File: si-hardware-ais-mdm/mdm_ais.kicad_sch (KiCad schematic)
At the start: 11 parts, among them U3 Si4362, Y1 30MHz

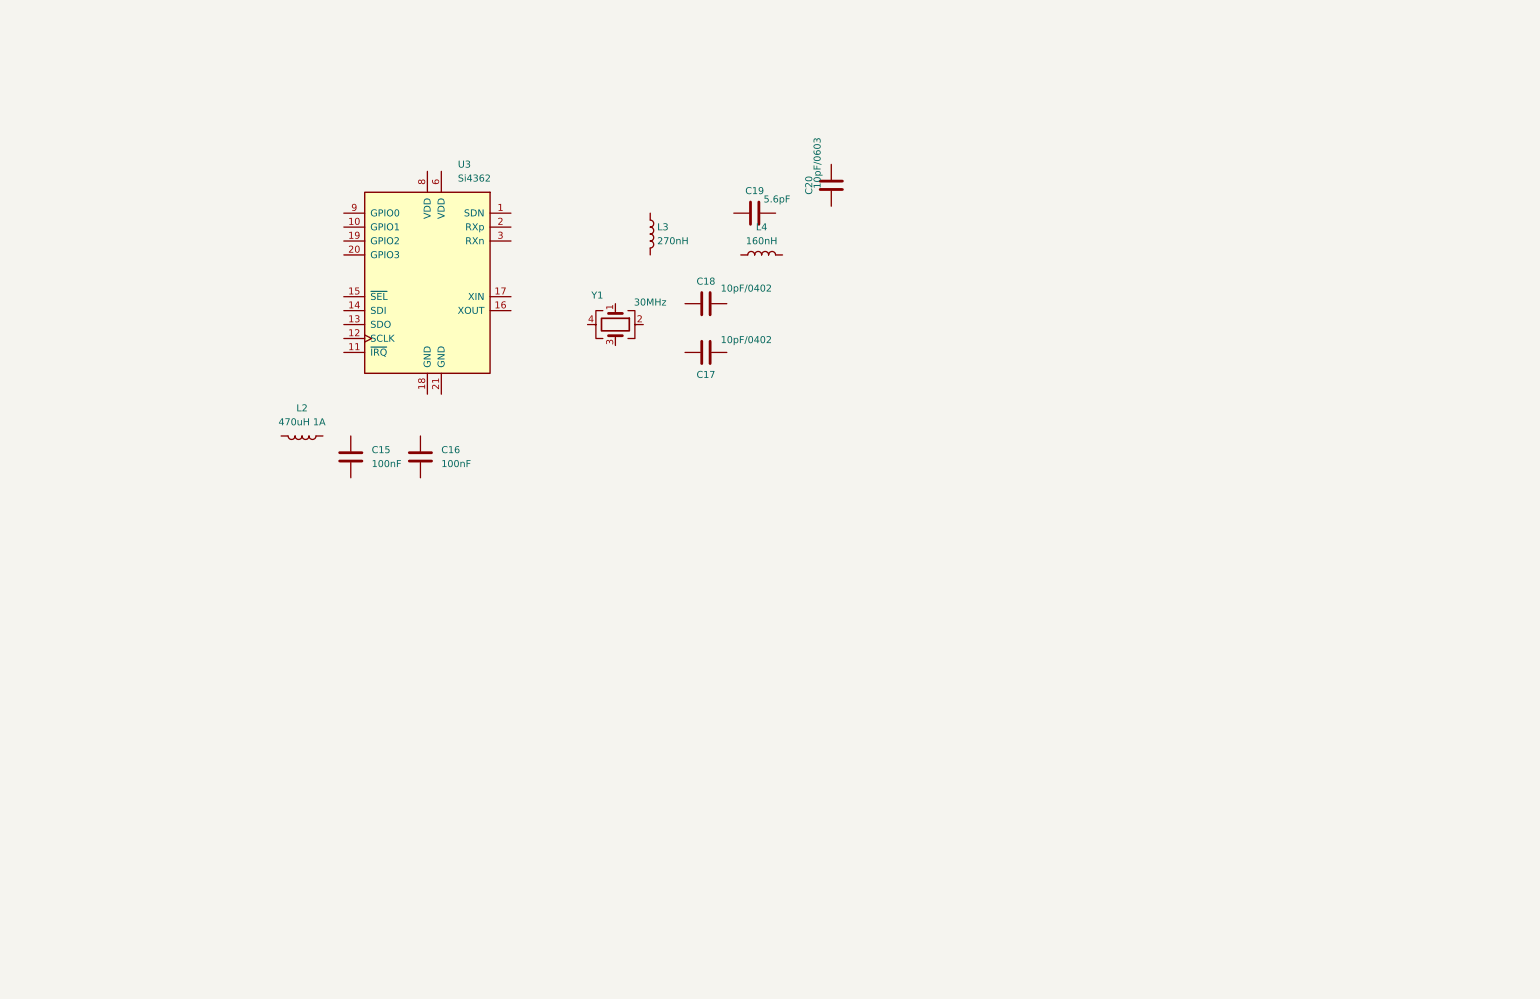
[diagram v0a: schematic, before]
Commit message: added function power input battery chargger mdm_ais
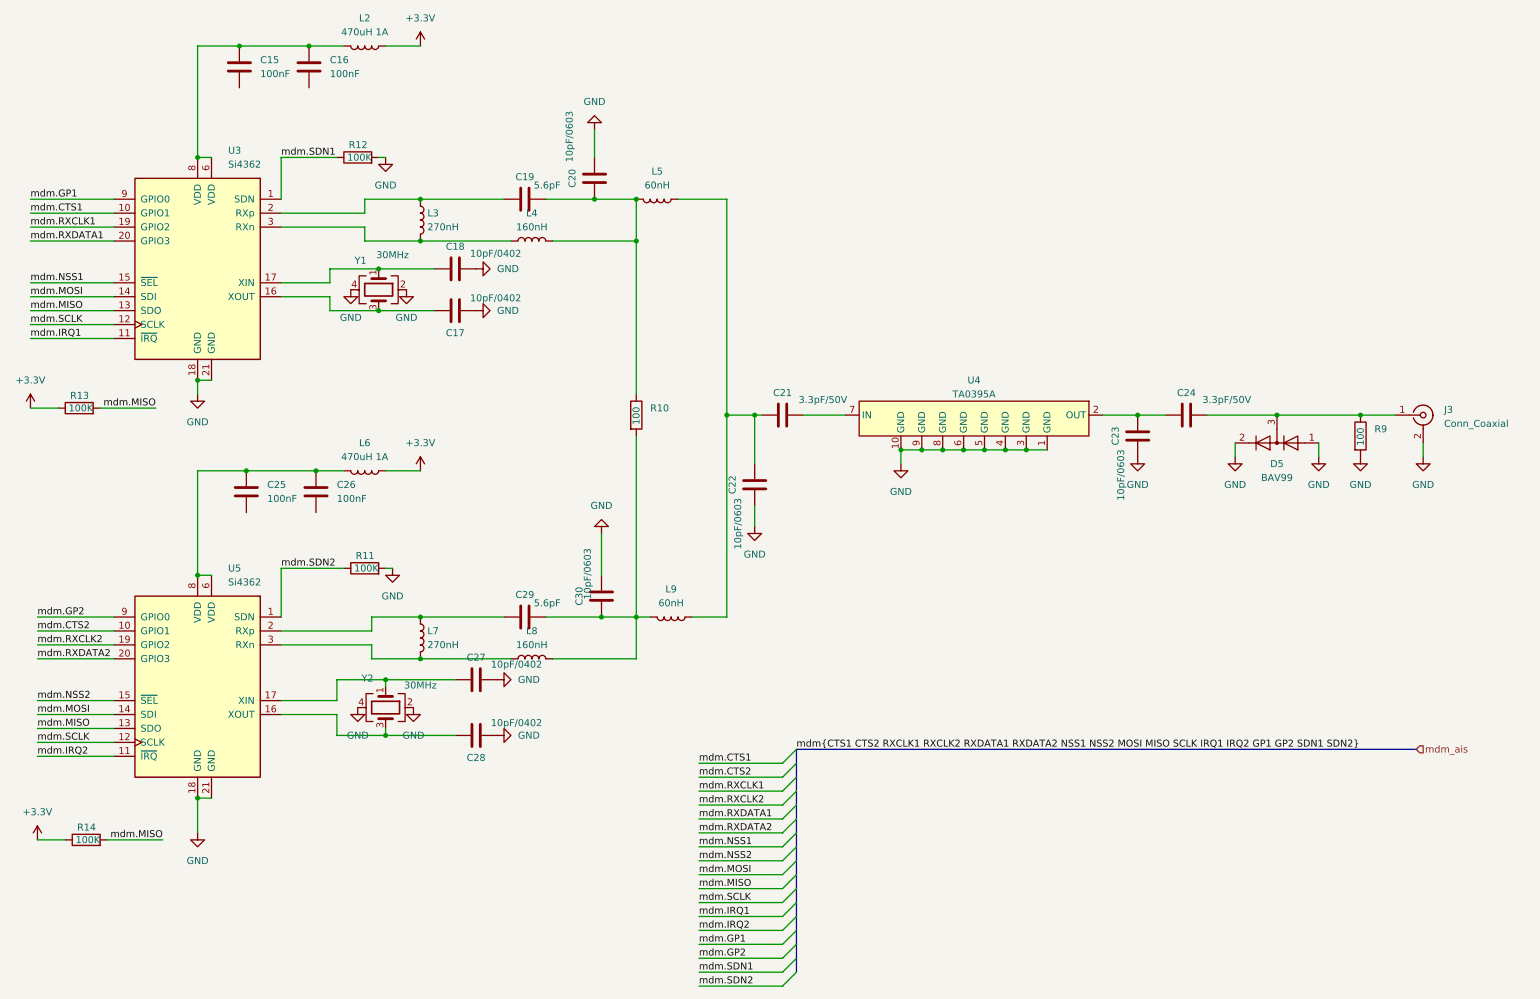
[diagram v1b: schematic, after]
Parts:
- added C21, C24: 3.3pF/50V, CTS_Capacitor_SMD:C_0603_1608Metric, symbol Device:C
- added C22, C23, C30: 10pF/0603, Capacitor_SMD:C_0603_1608Metric, symbol Device:C
- added C25, C26: 100nF, CTS_Capacitor_SMD:C_0402_1005Metric, symbol Device:C
- added C27, C28: 10pF/0402, CTS_Capacitor_SMD:C_0402_1005Metric, symbol Device:C
- added C29: 5.6pF, Capacitor_SMD:C_0805_2012Metric, symbol Device:C
- added D5: BAV99, Package_TO_SOT_SMD:SOT-23, symbol Diode:BAV99
- added J3: Conn_Coaxial, Connector_Coaxial:SMA_Molex_73251-1153_EdgeMount_Horizontal, symbol Connector:Conn_Coaxial
- added L5, L9: 60nH, SI_Inductor:RF_Inductor, symbol Device:L
- added L6: 470uH 1A, CTS_Inductor_SMD:Inductor_4.7x4.7mm_H3.0mm, symbol Device:L
- added L7: 270nH, Inductor_SMD:L_0603_1608Metric, symbol Device:L
- added L8: 160nH, Inductor_SMD:L_0603_1608Metric, symbol Device:L
- added R10, R9: 100, CTS_Resistor_SMD:R_0603_1608Metric, symbol Device:R
- added R11, R12, R13, R14: 100K, CTS_Resistor_SMD:R_0603_1608Metric, symbol Device:R
- added U4: TA0395A, SI_RF_FILTER:TA0395A, symbol SI_RF_FILTER:RF_FILTER
- added U5: Si4362, Package_DFN_QFN:QFN-20-1EP_4x4mm_P0.5mm_EP2.5x2.5mm, symbol RF_AM_FM:Si4362
- added Y2: 30MHz, Crystal:Crystal_SMD_3225-4Pin_3.2x2.5mm_HandSoldering, symbol Device:Crystal_GND24
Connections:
- net at Y1.1: now also C18.2, U3.17 (XIN)
- net GND: now reaches Y1.2
- net GND: now also C17.2, C18.1, C20.1, U3.18 (GND), U3.21 (GND), Y1.4, C22.2, C23.2, C27.1, C28.2, C30.1, D5.1 (K), D5.2 (A), J3.2 (Ext), R11.2, R12.2, R9.2, U4.1 (GND), U4.10 (GND), U4.3 (GND), U4.4 (GND), U4.5 (GND), U4.6 (GND), U4.8 (GND), U4.9 (GND), U5.18 (GND), U5.21 (GND), Y2.2, Y2.4
- net at Y1.3: now also C17.1, U3.16 (XOUT)
- net +3.3V: now reaches L2.1
- net +3.3V: now also L6.1, R13.1, R14.1
- net at L2.2: now also C15.1, C16.1, U3.6 (VDD), U3.8 (VDD)
- net at C20.2: now also C19.1, L4.2, L5.2, R10.1
- net at C19.2: now also L3.1, U3.2 (RXp)
- net at L3.2: now also L4.1, U3.3 (RXn)
- net mdm.SDN1: now reaches U3.1 (SDN)
- net mdm.SDN1: now also R12.1
- net mdm.CTS1: now reaches U3.10 (GPIO1)
- net mdm.IRQ1: now reaches U3.11 (~{IRQ})
- net mdm.SCLK: now reaches U3.12 (SCLK)
- net mdm.SCLK: now also U5.12 (SCLK)
- net mdm.MISO: now reaches U3.13 (SDO)
- net mdm.MISO: now also R13.2, R14.2, U5.13 (SDO)
- net mdm.MOSI: now reaches U3.14 (SDI)
- net mdm.MOSI: now also U5.14 (SDI)
- net mdm.NSS1: now reaches U3.15 (~{SEL})
- net mdm.RXCLK1: now reaches U3.19 (GPIO2)
- net mdm.RXDATA1: now reaches U3.20 (GPIO3)
- net mdm.GP1: now reaches U3.9 (GPIO0)
- new net: C29.2, L7.1, U5.2 (RXp)
- new net: L7.2, L8.1, U5.3 (RXn)
- new net: C29.1, C30.2, L8.2, L9.2, R10.2
- new net: C23.1, C24.2, U4.2 (OUT)
- new net: C21.1, U4.7 (IN)
- new net: C27.2, U5.17 (XIN), Y2.1
- new net: C28.1, U5.16 (XOUT), Y2.3
- new net: C21.2, C22.1, L5.1, L9.1
- new net: C25.1, C26.1, L6.2, U5.6 (VDD), U5.8 (VDD)
- new net: C24.1, D5.3 (K), J3.1 (In), R9.1
- new net mdm.CTS2: U5.10 (GPIO1)
- new net mdm.GP2: U5.9 (GPIO0)
- new net mdm.IRQ2: U5.11 (~{IRQ})
- new net mdm.NSS2: U5.15 (~{SEL})
- new net mdm.RXCLK2: U5.19 (GPIO2)
- new net mdm.RXDATA2: U5.20 (GPIO3)
- new net mdm.SDN2: R11.1, U5.1 (SDN)
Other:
- moved on the sheet: C15, C16, C17, C18, C19, C20, L2, L3, L4, U3, Y1

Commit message: schematic  to pcb
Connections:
- net GND: now also C15.2, C16.2, C25.2, C26.2

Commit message: layout and routing
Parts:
- removed R14: 100K, CTS_Resistor_SMD:R_0603_1608Metric, symbol Device:R
- L2, L6: value 470uH 1A -> 59uH 1A; footprint CTS_Inductor_SMD:Inductor_4.7x4.7mm_H3.0mm -> Capacitor_SMD:C_0402_1005Metric
- L5, L9: value 60nH -> 62nH; footprint SI_Inductor:RF_Inductor -> Inductor_SMD:L_0603_1608Metric; Order https://www.mouser.com/ProductDetail/Delevan/4726-60?qs=sGA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 -> https://www.mouser.tw/ProductDetail/Murata-Electronics/LQW1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
- Y1, Y2: footprint Crystal:Crystal_SMD_3225-4Pin_3.2x2.5mm_HandSoldering -> Crystal:Crystal_SMD_SeikoEpson_TSX3225-4Pin_3.2x2.5mm
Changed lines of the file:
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@@
 	(wire
 		(pts
-			(xy 33.02 165.1) (xy 43.18 165.1)
-		)
-		(stroke
-			(width 0)
-			(type default)
-		)
-	)
-	(wire
-		(pts
 			(xy 177.8 93.98) (xy 177.8 96.52)
 		)
@@
 	(wire
 		(pts
-			(xy 20.32 165.1) (xy 25.4 165.1)
-		)
-		(stroke
-			(width 0)
-			(type default)
-		)
-	)
-	(wire
-		(pts
 			(xy 20.32 127) (xy 34.29 127)
 		)
@@
 		)
 	)
-	(label "mdm.MISO"
-		(at 43.18 165.1 180)
-		(fields_autoplaced yes)
-		(effects
-			(font
-				(size 1.27 1.27)
-			)
-			(justify right bottom)
-		)
-	)
 	(label "mdm.MOSI"
 		(at 19.05 66.04 0)
@@
 			)
 		)
-		(property "Footprint" "Crystal:Crystal_SMD_3225-4Pin_3.2x2.5mm_HandSoldering"
+		(property "Footprint" "Crystal:Crystal_SMD_SeikoEpson_TSX3225-4Pin_3.2x2.5mm"
 			(at 83.82 140.97 0)
 			(effects
@@
 			)
 		)
-		(property "Value" "60nH"
+		(property "Value" "62nH"
 			(at 133.35 45.72 90)
 			(effects
@@
 			)
 		)
-		(property "Footprint" "SI_Inductor:RF_Inductor"
+		(property "Footprint" "Inductor_SMD:L_0603_1608Metric"
 			(at 133.35 48.26 0)
 			(effects
@@
 			)
 		)
-		(property "Order" "https://www.mouser.com/ProductDetail/Delevan/4726-60?qs=sGAEpiMZZMv126LJFLh8y%252BHwvErnD0xOHz%252Br%2F%2FsVKBI%3D"
+		(property "Order" "https://www.mouser.tw/ProductDetail/Murata-Electronics/LQW18AN62NJ0ZD?qs=Ey7%2FXF42M3fv0gXJTm%2FnKQ%3D%3D"
 			(at 133.35 48.26 90)
 			(effects
@@
 			)
 		)
-		(property "Footprint" "Crystal:Crystal_SMD_3225-4Pin_3.2x2.5mm_HandSoldering"
+		(property "Footprint" "Crystal:Crystal_SMD_SeikoEpson_TSX3225-4Pin_3.2x2.5mm"
 			(at 82.55 64.77 0)
 			(effects
@@
 			)
 		)
-		(property "Value" "470uH 1A"
+		(property "Value" "59uH 1A"
 			(at 80.01 17.78 90)
 			(effects
@@
 			)
 		)
-		(property "Footprint" "CTS_Inductor_SMD:Inductor_4.7x4.7mm_H3.0mm"
+		(property "Footprint" "Capacitor_SMD:C_0402_1005Metric"
 			(at 80.01 20.32 0)
 			(effects
@@
 	)
 	(symbol
-		(lib_id "power:+3.3V")
-		(at 20.32 165.1 0)
-		(unit 1)
-		(exclude_from_sim no)
-		(in_bom yes)
-		(on_board yes)
-		(dnp no)
-		(fields_autoplaced yes)
-		(property "Reference" "#PWR04"
-			(at 20.32 168.91 0)
-			(effects
-				(font
-					(size 1.27 1.27)
-				)
-				(hide yes)
-			)
-		)
-		(property "Value" "+3.3V"
-			(at 20.32 160.02 0)
-			(effects
-				(font
-					(size 1.27 1.27)
-				)
-			)
-		)
-		(property "Footprint" ""
-			(at 20.32 165.1 0)
-			(effects
-				(font
-					(size 1.27 1.27)
-				)
-				(hide yes)
-			)
-		)
-		(property "Datasheet" ""
-			(at 20.32 165.1 0)
-			(effects
-				(font
-					(size 1.27 1.27)
-				)
-				(hide yes)
-			)
-		)
-		(property "Description" "Power symbol creates a global label with name \"+3.3V\""
-			(at 20.32 165.1 0)
-			(effects
-				(font
-					(size 1.27 1.27)
-				)
-				(hide yes)
-			)
-		)
-		(pin "1"
-		)
-		(instances
-			(project "si-hardware-ais-mdm"
-				(path "/97f80214-d5cc-4a35-9cac-bb1ff8330c6a/5ae8db80-f83d-460f-bd68-cb2ce4c023ac"
-					(reference "#PWR04")
-					(unit 1)
-				)
-			)
-		)
-	)
-	(symbol
 		(lib_id "Device:R")
 		(at 78.74 40.64 90)
@@
 			)
 		)
-		(property "Value" "470uH 1A"
+		(property "Value" "59uH 1A"
 			(at 80.01 95.25 90)
 			(effects
@@
 			)
 		)
-		(property "Footprint" "CTS_Inductor_SMD:Inductor_4.7x4.7mm_H3.0mm"
+		(property "Footprint" "Capacitor_SMD:C_0402_1005Metric"
 			(at 80.01 97.79 0)
 			(effects
@@
 	)
 	(symbol
-		(lib_id "Device:R")
-		(at 29.21 165.1 90)
-		(unit 1)
-		(exclude_from_sim no)
-		(in_bom yes)
-		(on_board yes)
-		(dnp no)
-		(property "Reference" "R14"
-			(at 30.988 162.814 90)
-			(effects
-				(font
-					(size 1.27 1.27)
-				)
-				(justify left)
-			)
-		)
-		(property "Value" "100K"
-			(at 31.75 165.1 90)
-			(effects
-				(font
-					(size 1.27 1.27)
-				)
-				(justify left)
-			)
-		)
-		(property "Footprint" "CTS_Resistor_SMD:R_0603_1608Metric"
-			(at 29.21 166.878 90)
-			(effects
-				(font
-					(size 1.27 1.27)
-				)
-				(hide yes)
-			)
-		)
-		(property "Datasheet" "~"
-			(at 29.21 165.1 0)
-			(effects
-				(font
-					(size 1.27 1.27)
-				)
-				(hide yes)
-			)
-		)
-		(property "Description" "Resistor"
-			(at 29.21 165.1 0)
-			(effects
-				(font
-					(size 1.27 1.27)
-				)
-				(hide yes)
-			)
-		)
-		(pin "1"
-		)
-		(pin "2"
-		)
-		(instances
-			(project "si-hardware-ais-mdm"
-				(path "/97f80214-d5cc-4a35-9cac-bb1ff8330c6a/5ae8db80-f83d-460f-bd68-cb2ce4c023ac"
-					(reference "R14")
-					(unit 1)
-				)
-			)
-		)
-	)
-	(symbol
 		(lib_id "power:GND")
 		(at 78.74 140.97 0)
@@
 			)
 		)
-		(property "Value" "60nH"
+		(property "Value" "62nH"
 			(at 135.89 121.92 90)
 			(effects
@@
 			)
 		)
-		(property "Footprint" "SI_Inductor:RF_Inductor"
+		(property "Footprint" "Inductor_SMD:L_0603_1608Metric"
 			(at 135.89 124.46 0)
 			(effects
@@
 			)
 		)
-		(property "Order" "https://www.mouser.com/ProductDetail/Delevan/4726-60?qs=sGAEpiMZZMv126LJFLh8y%252BHwvErnD0xOHz%252Br%2F%2FsVKBI%3D"
+		(property "Order" "https://www.mouser.tw/ProductDetail/Murata-Electronics/LQW18AN62NJ0ZD?qs=Ey7%2FXF42M3fv0gXJTm%2FnKQ%3D%3D"
 			(at 135.89 124.46 90)
 			(effects

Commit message: added schematic pdf
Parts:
- L2, L6: value 59uH 1A -> 59nH 1A
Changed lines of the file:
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@@
 			)
 		)
-		(property "Value" "59uH 1A"
+		(property "Value" "59nH 1A"
 			(at 80.01 17.78 90)
 			(effects
@@
 			)
 		)
-		(property "Value" "59uH 1A"
+		(property "Value" "59nH 1A"
 			(at 80.01 95.25 90)
 			(effects
